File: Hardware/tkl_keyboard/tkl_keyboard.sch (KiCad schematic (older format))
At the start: 0 parts

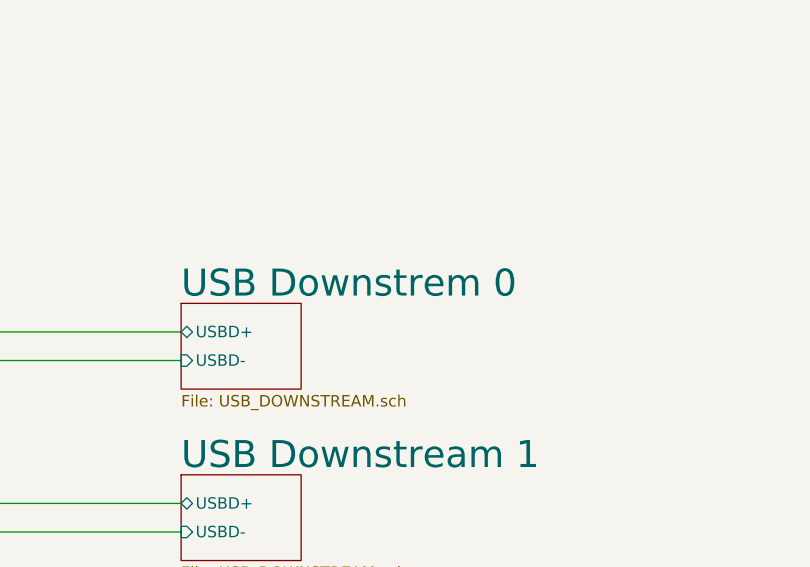
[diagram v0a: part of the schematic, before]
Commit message: LEDs and diodes routed
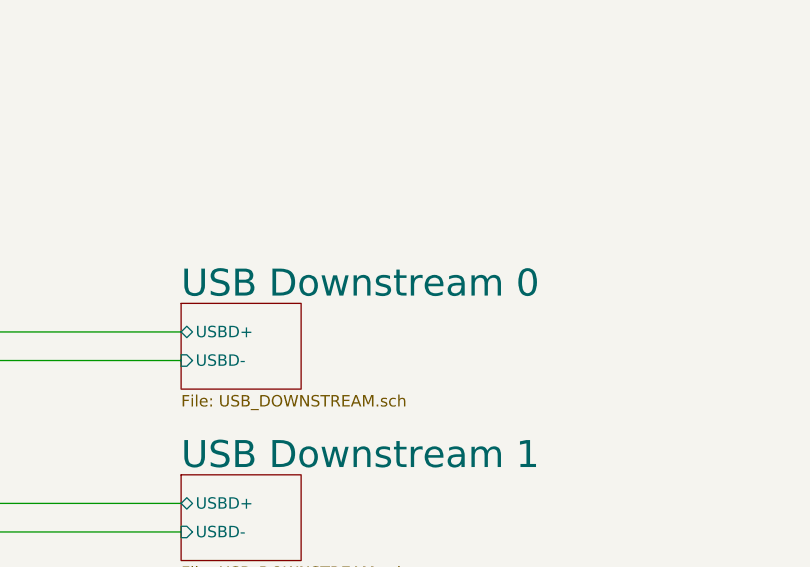
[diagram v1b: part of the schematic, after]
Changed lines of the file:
@@
 S 8375 2825 525  375
 U 650FF941
-F0 "USB Downstrem 0" 118
+F0 "USB Downstream 0" 118
 F1 "USB_DOWNSTREAM.sch" 50
 F2 "USBD+" B L 8375 2950 50

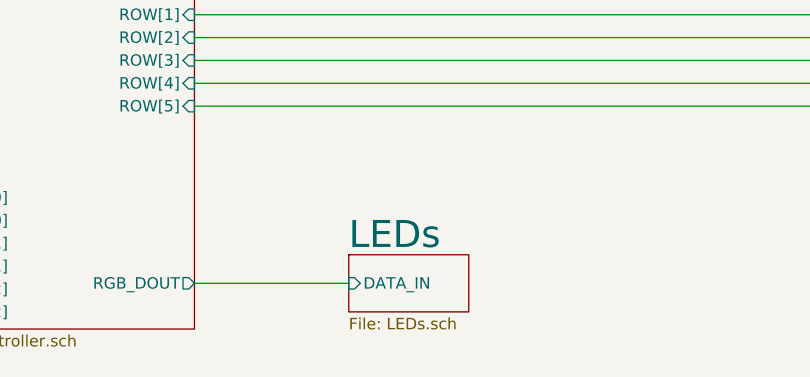
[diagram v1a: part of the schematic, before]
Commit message: Rows and columns routed to controller. Extended top board edge to fit OLED. Removed optional resistors around CMC.
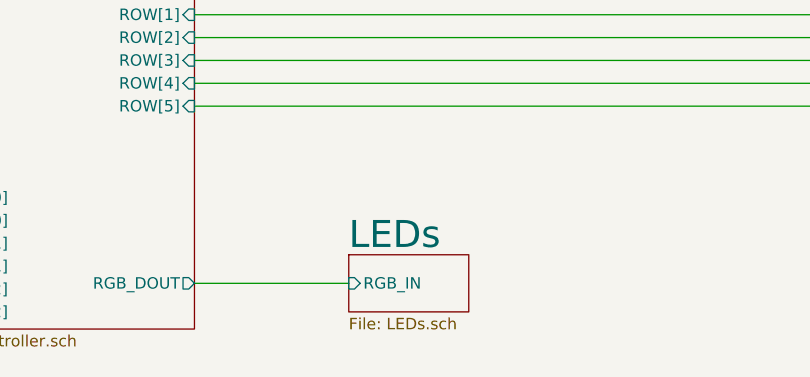
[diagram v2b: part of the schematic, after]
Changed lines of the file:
@@
 F0 "LEDs" 118
 F1 "LEDs.sch" 50
-F2 "DATA_IN" I L 10050 8525 50
+F2 "RGB_IN" I L 10050 8525 50
 $EndSheet
 $Sheet

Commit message: Updating schematic
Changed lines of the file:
@@
 $Descr A3 16535 11693
 encoding utf-8
-Sheet 1 11
+Sheet 1 12
 Title ""
 Date ""
@@
 Text Notes 750  1000 0    315  ~ 0
 TKL KEYBOARD
+$Sheet
+S 2125 6975 1650 700
+U 613390DE
+F0 "Power" 118
+F1 "Power.sch" 50
+$EndSheet
 $EndSCHEMATC

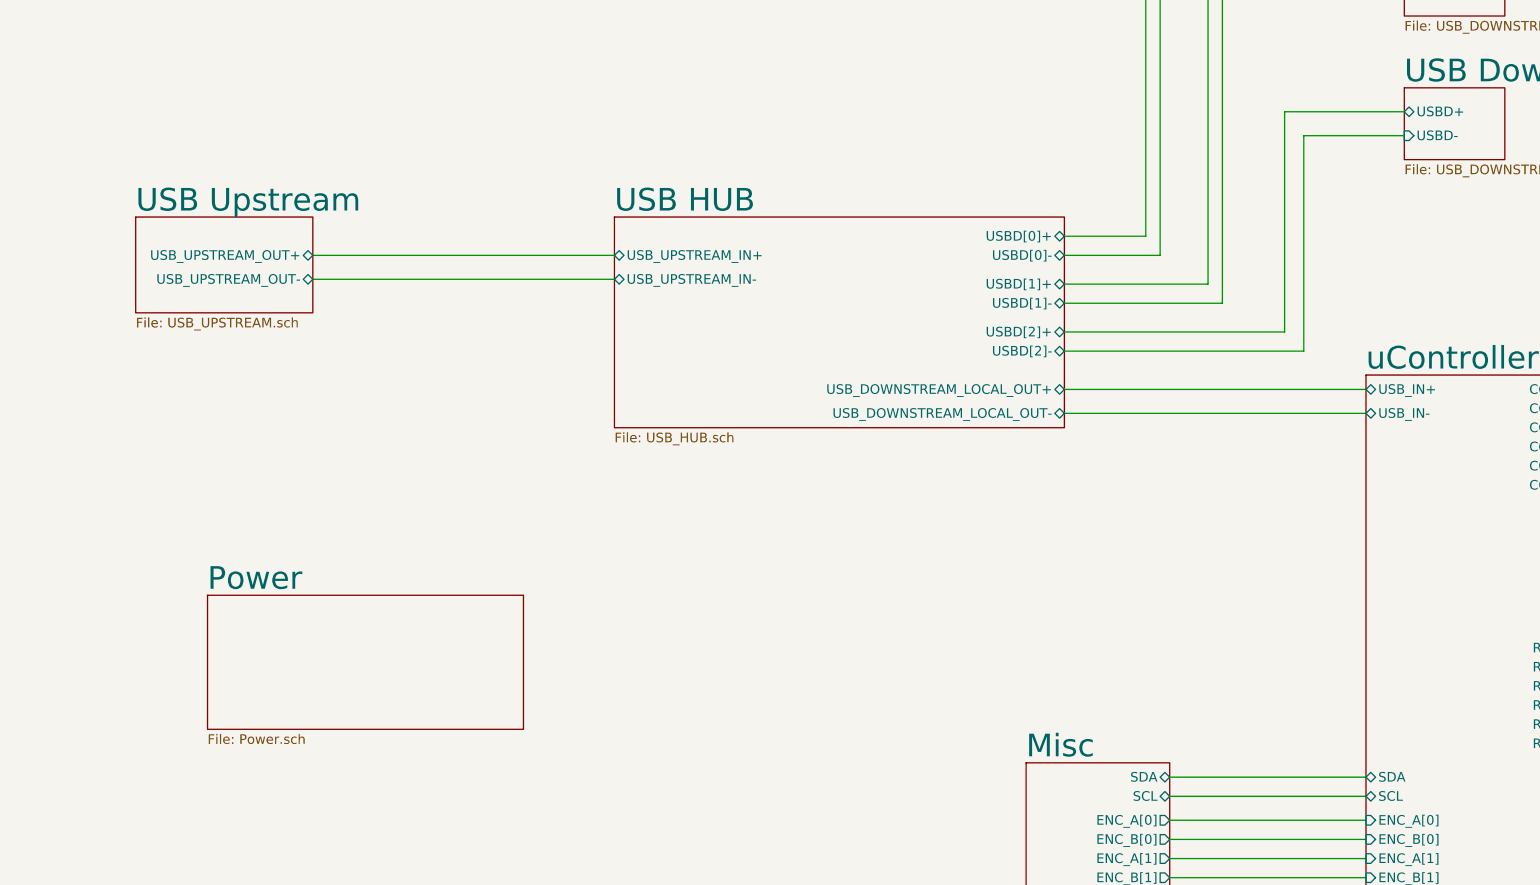
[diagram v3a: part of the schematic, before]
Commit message: Tidying schematic
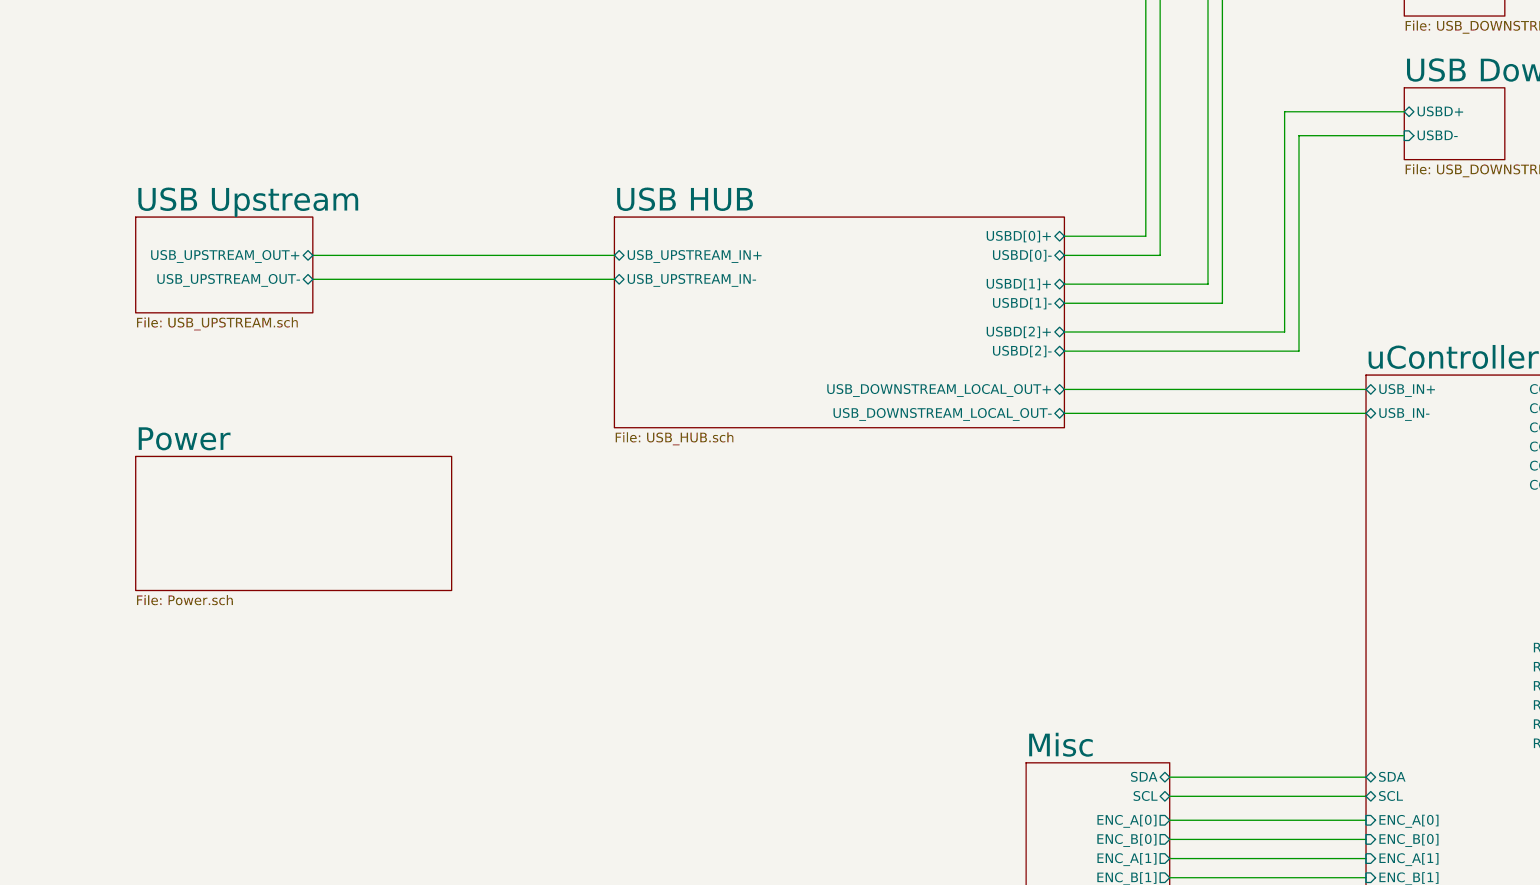
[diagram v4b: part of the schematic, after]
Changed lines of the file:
@@
 encoding utf-8
 Sheet 1 12
-Title ""
+Title "TKL Keyboard"
 Date ""
-Rev ""
+Rev "0"
 Comp ""
 Comment1 ""
@@
 	7750 4450 8375 4450
 Wire Wire Line
-	6600 5700 7850 5700
-Wire Wire Line
-	7850 5700 7850 4575
-Wire Wire Line
-	7850 4575 8375 4575
+	6600 5700 7825 5700
 Text Notes 750  1000 0    315  ~ 0
 TKL KEYBOARD
 $Sheet
-S 2125 6975 1650 700
+S 1750 6250 1650 700
 U 613390DE
 F0 "Power" 118
 F1 "Power.sch" 50
 $EndSheet
+Wire Wire Line
+	7825 5700 7825 4575
+Wire Wire Line
+	7825 4575 8375 4575
 $EndSCHEMATC
